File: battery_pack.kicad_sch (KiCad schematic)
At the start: 4 parts

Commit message: usb pd charging
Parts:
- added BT5: Battery_Cell, symbol Device:Battery_Cell
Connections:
- net CELL4: now also BT5.2 (-)
- new net CELL5: BT5.1 (+)
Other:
- moved on the sheet: BT1, BT2, BT3, BT4

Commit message: progress
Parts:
- removed BT1, BT2, BT3, BT4, BT5: Battery_Cell, symbol Device:Battery_Cell
- added BT1, BT2, BT3, BT4, BT5: 1106, 26650_cell_holder:BAT_1106, symbol 1106_26650_Cell_Holder:1106
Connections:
- net CELL1: now also BT4.N, BT5.P
- net CELL2: now also BT3.N, BT4.P
- net CELL3: now also BT2.N, BT3.P
- net CELL4: now also BT1.N, BT2.P
- new net BATT+: BT1.P
- new net BATT-: BT5.N

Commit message: structural changes
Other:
- note added: "Cell Datasheet : https://www.allbatteries.co.uk/media/pdf/ACL9089_UK.pdf"
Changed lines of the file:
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@@
 	(generator_version "9.0")
 	(paper "A4")
-	(rectangle
-		(start 97.79 49.53)
-		(end 130.81 147.32)
-		(stroke
-			(width 0)
-			(type default)
-		)
-		(fill
-			(type none)
+	(text "Cell Datasheet : https://www.allbatteries.co.uk/media/pdf/ACL9089_UK.pdf"
+		(exclude_from_sim no)
+		(at 92.456 45.212 0)
+		(effects
+			(font
+				(size 1.27 1.27)
+			)
 		)
 	)

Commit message: development stage 1 - testing board for AFE / Fuel gage / high side protection controller - unfinished
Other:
- note added: "Cell Datasheet :"
- note added: "https://www.allbatteries.co.uk/media/pdf/ACL9089_UK.pdf"
- note removed: "Cell Datasheet : https://www.allbatteries.co.uk/media/pdf/ACL9089_UK.pdf"
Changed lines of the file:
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@@
 	(generator_version "9.0")
 	(paper "A4")
-	(text "Cell Datasheet : https://www.allbatteries.co.uk/media/pdf/ACL9089_UK.pdf"
+	(text "https://www.allbatteries.co.uk/media/pdf/ACL9089_UK.pdf"
 		(exclude_from_sim no)
-		(at 92.456 45.212 0)
+		(at 67.31 49.53 0)
 		(effects
 			(font
+				(size 1.27 1.27)
+			)
+		)
+	)
+	(text "Cell Datasheet : "
+		(exclude_from_sim no)
+		(at 50.8 45.72 0)
+		(effects
+			(font

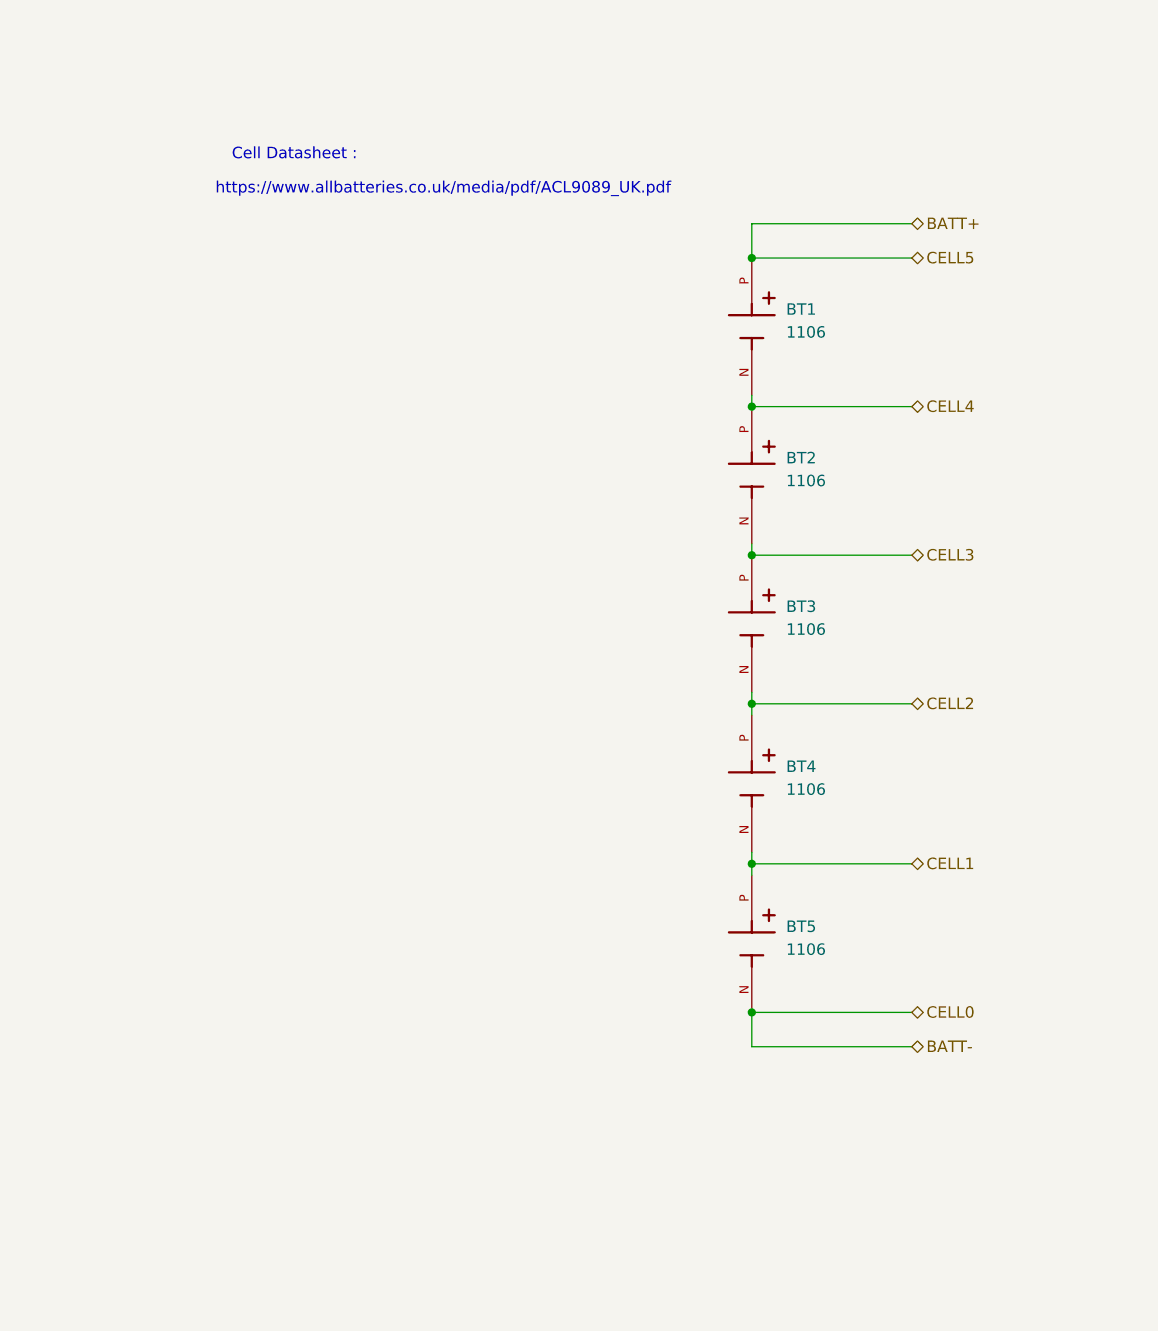
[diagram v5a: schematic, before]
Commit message: refinements - moving battery pack off the PCB
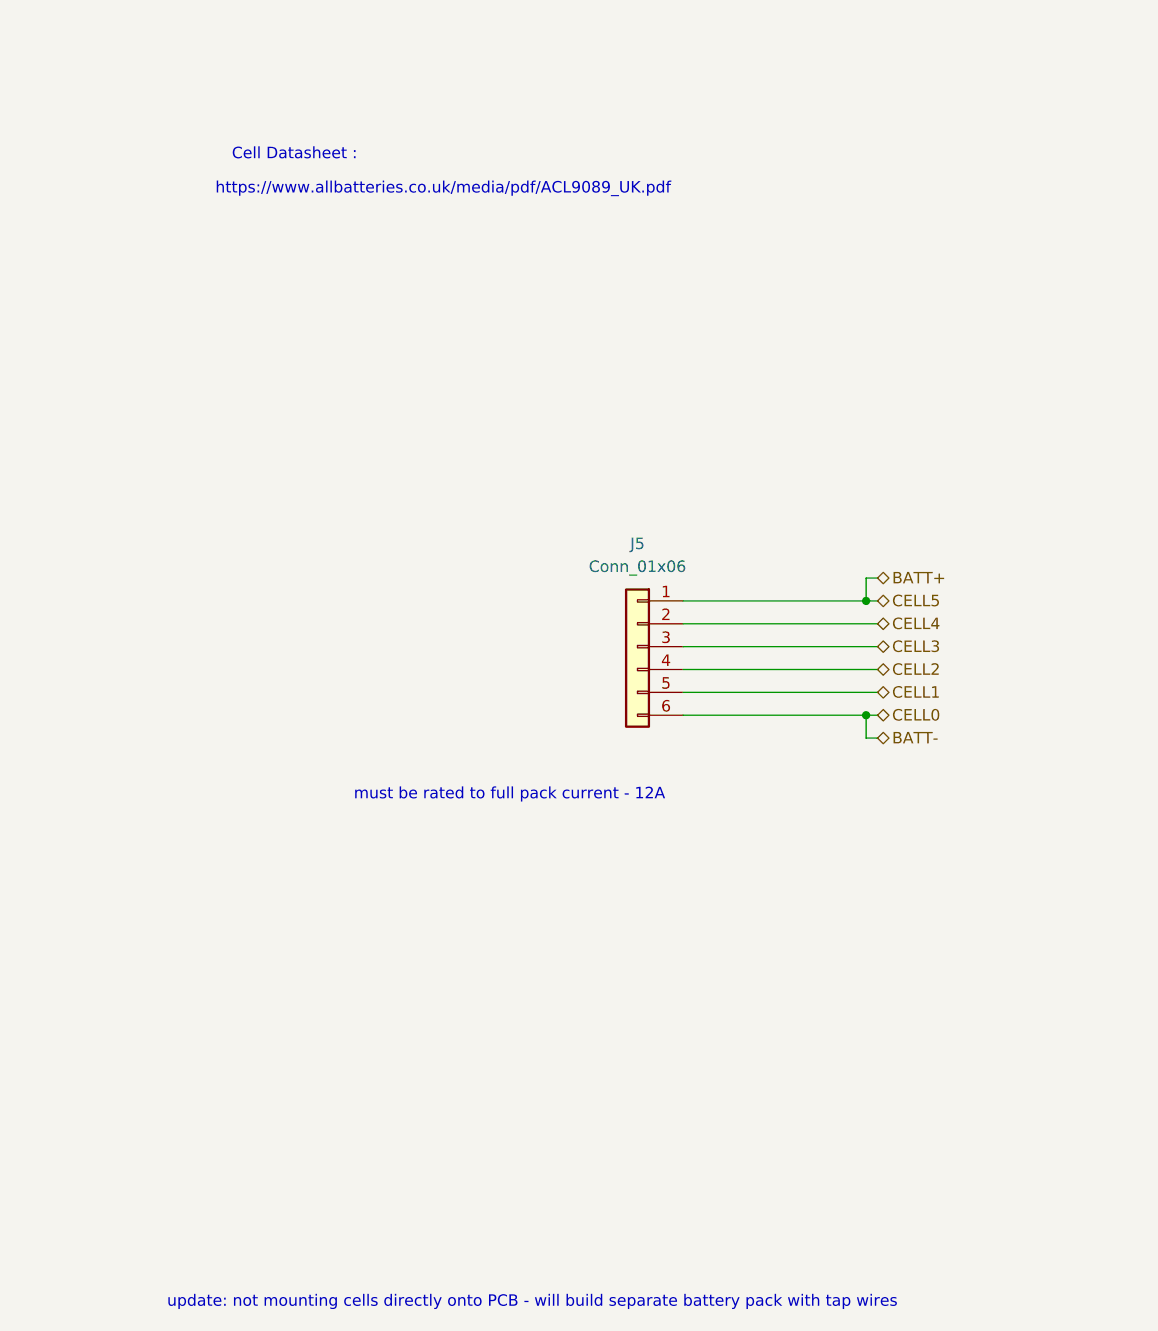
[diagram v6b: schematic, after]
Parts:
- removed BT1, BT2, BT3, BT4, BT5: 1106, 26650_cell_holder:BAT_1106, symbol 1106_26650_Cell_Holder:1106
- added J5: Conn_01x06, TerminalBlock_Phoenix:TerminalBlock_Phoenix_MKDS-1,5-6-5.08_1x06_P5.08mm_Horizontal, symbol Connector_Generic:Conn_01x06
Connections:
- net BATT+: now also J5.1 (Pin_1)
- net BATT-: now also J5.6 (Pin_6)
- net CELL1: now also J5.5 (Pin_5)
- net CELL2: now also J5.4 (Pin_4)
- net CELL3: now also J5.3 (Pin_3)
- net CELL4: now also J5.2 (Pin_2)
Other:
- note added: "must be rated to full pack current - 12A"
- note added: "update: not mounting cells directly onto PCB - will build separate battery pack with tap wires"

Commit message: adding charging stages finally
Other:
- note added: "batt pack physical construction ?"
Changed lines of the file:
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@@
 	(generator_version "9.0")
 	(paper "A4")
+	(circle
+		(center 70.866 164.338)
+		(radius 3.5921)
+		(stroke
+			(width 0)
+			(type default)
+		)
+		(fill
+			(type none)
+		)
+	)
+	(circle
+		(center 74.676 157.988)
+		(radius 1.27)
+		(stroke
+			(width 0)
+			(type default)
+		)
+		(fill
+			(type none)
+		)
+	)
+	(circle
+		(center 74.676 157.988)
+		(radius 3.5921)
+		(stroke
+			(width 0)
+			(type default)
+		)
+		(fill
+			(type none)
+		)
+	)
+	(arc
+		(start 70.866 164.338)
+		(mid 71.4559 160.3739)
+		(end 74.676 157.988)
+		(stroke
+			(width 0)
+			(type default)
+		)
+		(fill
+			(type none)
+		)
+	)
+	(circle
+		(center 82.296 157.988)
+		(radius 1.27)
+		(stroke
+			(width 0)
+			(type default)
+		)
+		(fill
+			(type none)
+		)
+	)
+	(circle
+		(center 67.056 157.988)
+		(radius 1.27)
+		(stroke
+			(width 0)
+			(type default)
+		)
+		(fill
+			(type none)
+		)
+	)
+	(circle
+		(center 82.296 157.988)
+		(radius 3.5921)
+		(stroke
+			(width 0)
+			(type default)
+		)
+		(fill
+			(type none)
+		)
+	)
+	(arc
+		(start 78.486 164.338)
+		(mid 79.0759 160.3739)
+		(end 82.296 157.988)
+		(stroke
+			(width 0)
+			(type default)
+		)
+		(fill
+			(type none)
+		)
+	)
+	(circle
+		(center 67.056 157.988)
+		(radius 3.5921)
+		(stroke
+			(width 0)
+			(type default)
+		)
+		(fill
+			(type none)
+		)
+	)
+	(arc
+		(start 67.056 157.988)
+		(mid 70.2761 160.3739)
+		(end 70.866 164.338)
+		(stroke
+			(width 0)
+			(type default)
+		)
+		(fill
+			(type none)
+		)
+	)
+	(arc
+		(start 74.676 157.988)
+		(mid 77.8961 160.3739)
+		(end 78.486 164.338)
+		(stroke
+			(width 0)
+			(type default)
+		)
+		(fill
+			(type none)
+		)
+	)
+	(circle
+		(center 78.486 164.338)
+		(radius 3.5921)
+		(stroke
+			(width 0)
+			(type default)
+		)
+		(fill
+			(type none)
+		)
+	)
 	(text "must be rated to full pack current - 12A"
 		(exclude_from_sim no)
@@
 		)
 	)
+	(text "batt pack physical construction ? "
+		(exclude_from_sim no)
+		(at 73.66 151.13 0)
+		(effects
+			(font
+				(size 1.27 1.27)
+			)
+		)
+	)
 	(text "update: not mounting cells directly onto PCB - will build separate battery pack with tap wires"
 		(exclude_from_sim no)
-		(at 77.216 173.228 0)
+		(at 80.01 146.05 0)
 		(effects
 			(font
